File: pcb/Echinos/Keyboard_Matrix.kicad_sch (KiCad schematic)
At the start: 40 parts, among them J5 Joystick

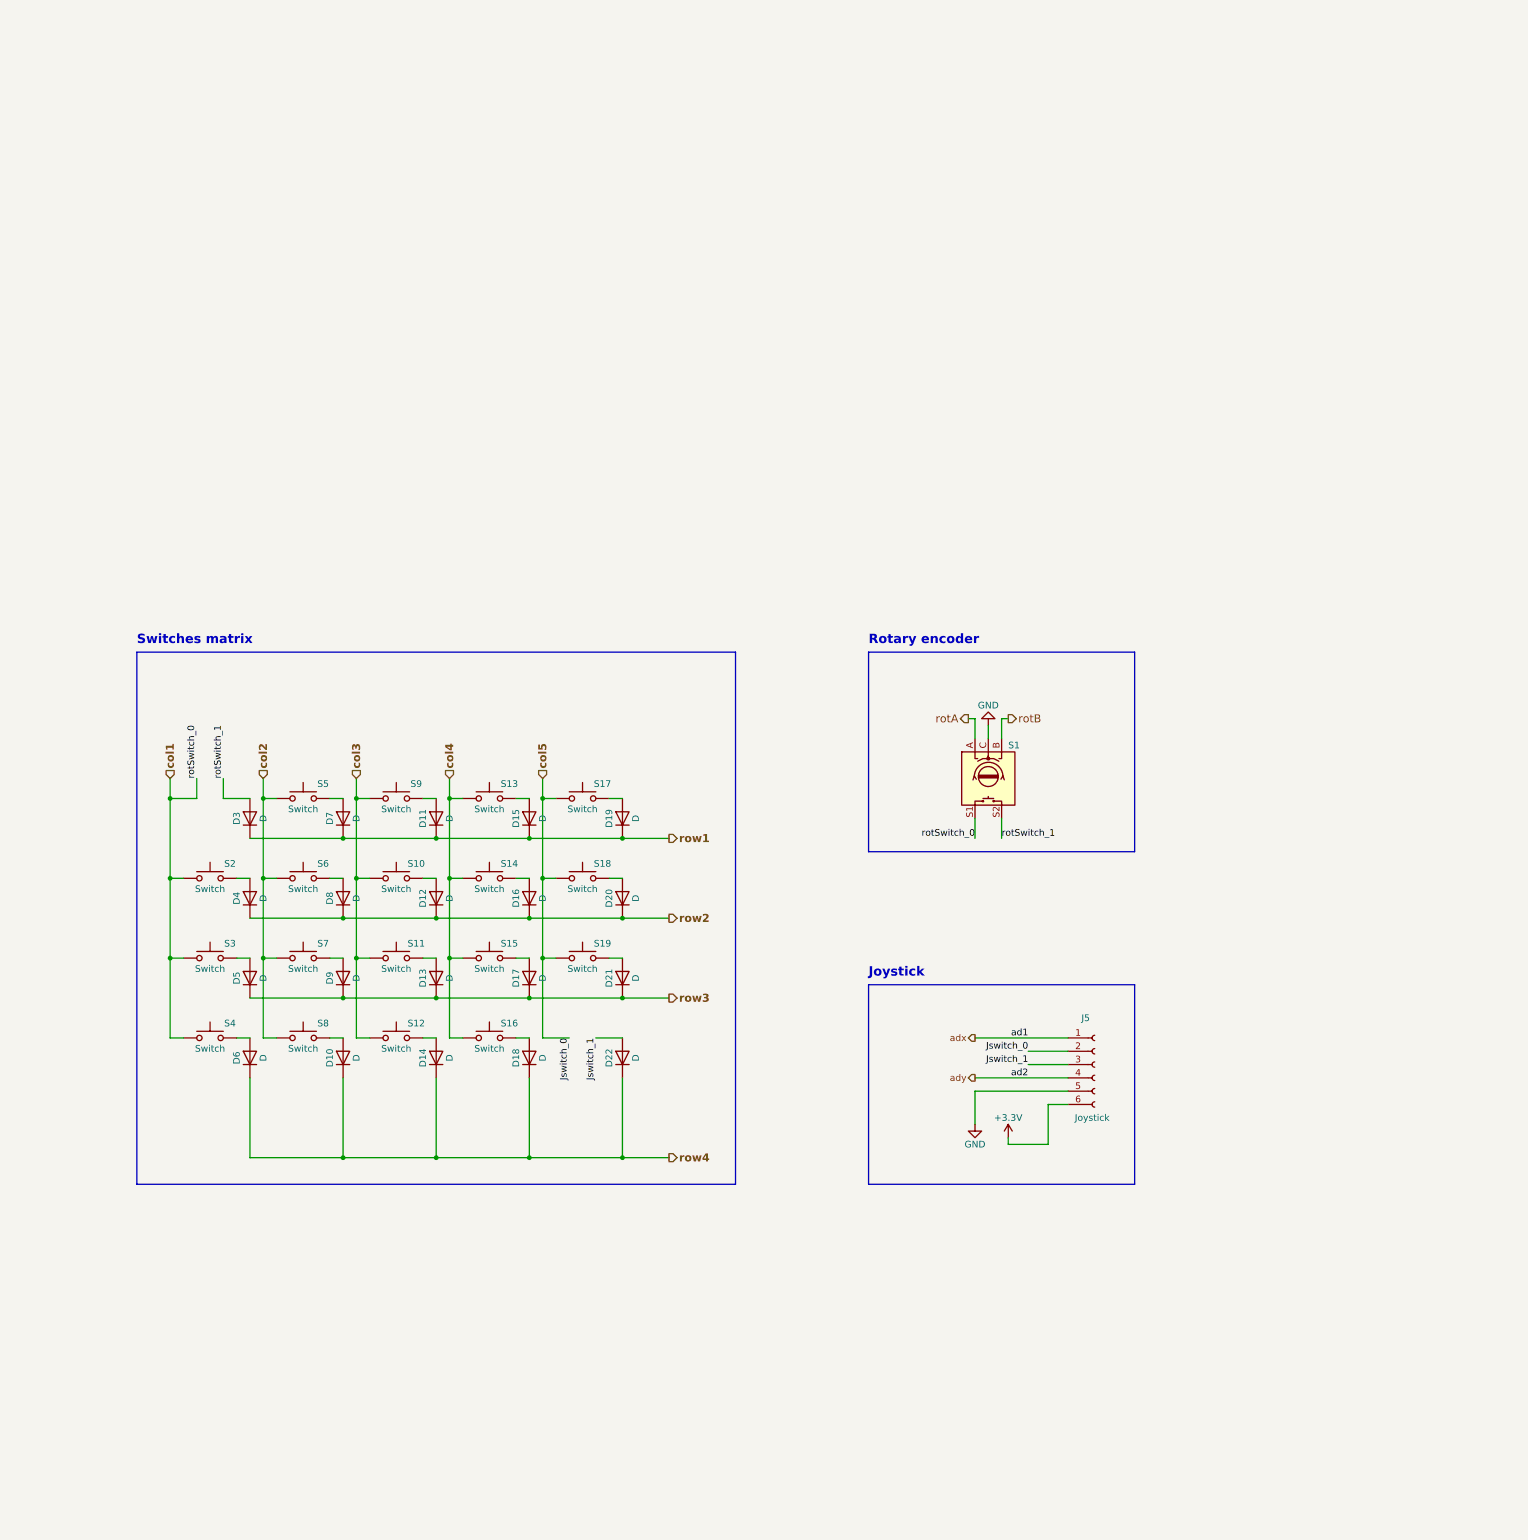
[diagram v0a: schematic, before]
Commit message: ✨ [PCB] - Continue draft schematic by adding per key RGB LED.
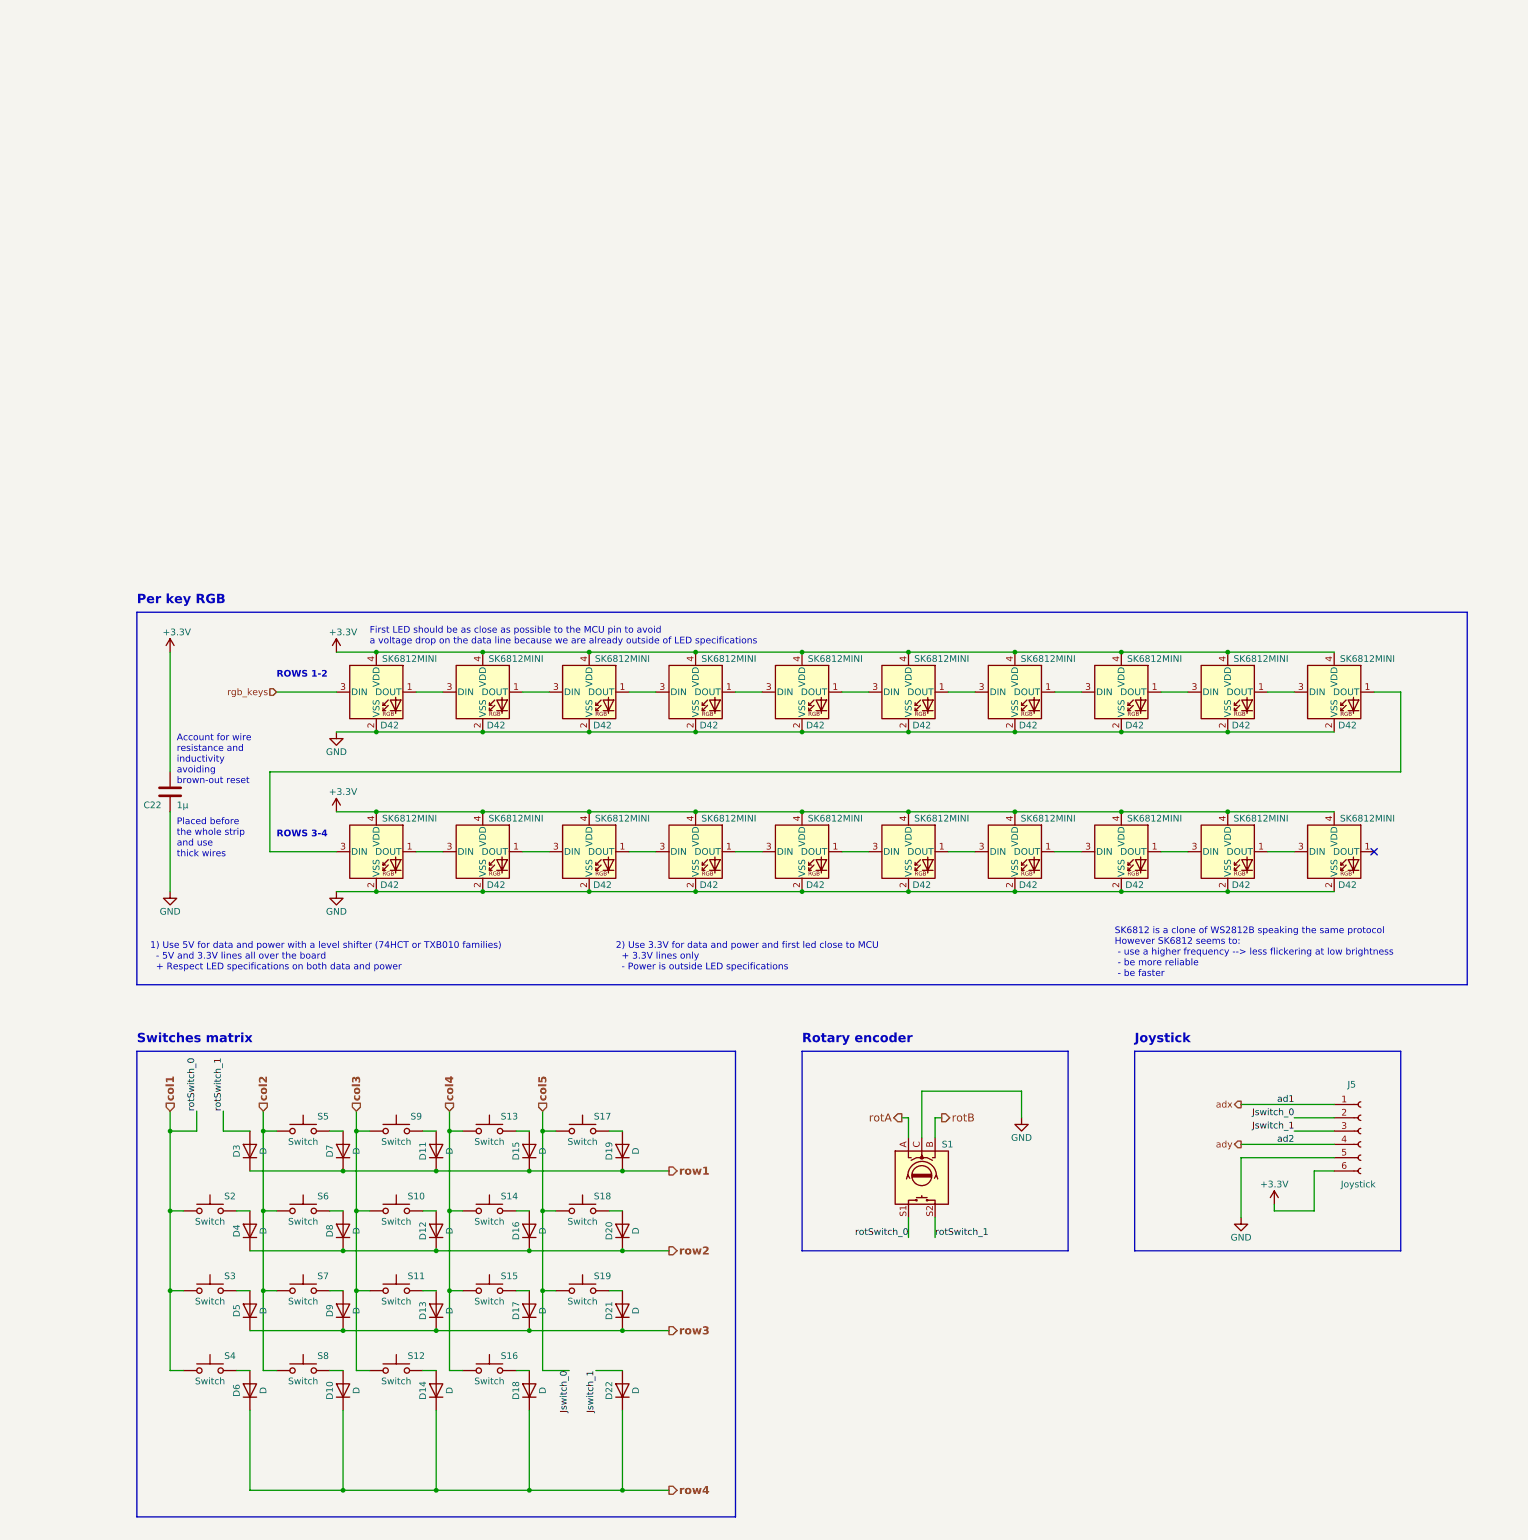
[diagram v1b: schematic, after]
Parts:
- added C22: 1µ, Capacitor_SMD:C_0402_1005Metric, symbol Device:C
- added D42 (x20): SK6812MINI, LED_SMD:LED_SK6812MINI_PLCC4_3.5x3.5mm_P1.75mm, symbol LED:SK6812MINI
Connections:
- net +3V3: now also C22.1, D42.4 (VDD), D42.4 (VDD), D42.4 (VDD), D42.4 (VDD), D42.4 (VDD), D42.4 (VDD), D42.4 (VDD), D42.4 (VDD), D42.4 (VDD), D42.4 (VDD), D42.4 (VDD), D42.4 (VDD), D42.4 (VDD), D42.4 (VDD), D42.4 (VDD), D42.4 (VDD), D42.4 (VDD), D42.4 (VDD), D42.4 (VDD), D42.4 (VDD)
- net GND: now also C22.2, D42.2 (VSS), D42.2 (VSS), D42.2 (VSS), D42.2 (VSS), D42.2 (VSS), D42.2 (VSS), D42.2 (VSS), D42.2 (VSS), D42.2 (VSS), D42.2 (VSS), D42.2 (VSS), D42.2 (VSS), D42.2 (VSS), D42.2 (VSS), D42.2 (VSS), D42.2 (VSS), D42.2 (VSS), D42.2 (VSS), D42.2 (VSS), D42.2 (VSS)
- new net: D42.1 (DOUT), D42.3 (DIN) (x19)
- new net rgb_keys: D42.3 (DIN)
- no-connect marks 0 -> 1
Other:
- note added: "1) Use 5V for data and power with a level shifter (74HCT or TXB010 families) - 5V and 3.3V lines all over the board + Respect LED specifications on both data and power"
- note added: "2) Use 3.3V for data and power and first led close to MCU + 3.3V lines only - Power is outside LED specifications"
- note added: "Account for wire resistance and inductivity avoiding brown-out reset"
- note added: "First LED should be as close as possible to the MCU pin to avoid a voltage drop on the data line because we are already outside of LED specifications"
- note added: "Per key RGB"
- note added: "Placed before the whole strip and use thick wires"
- note added: "ROWS 1-2"
- note added: "ROWS 3-4"
- note added: "SK6812 is a clone of WS2812B speaking the same protocol However SK6812 seems to: - use a higher frequency --> less flickering at low brightness - be more reliable - be faster"
- moved on the sheet: D10, D11, D12, D13, D14, D15, D16, D17, D18, D19, D20, D21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

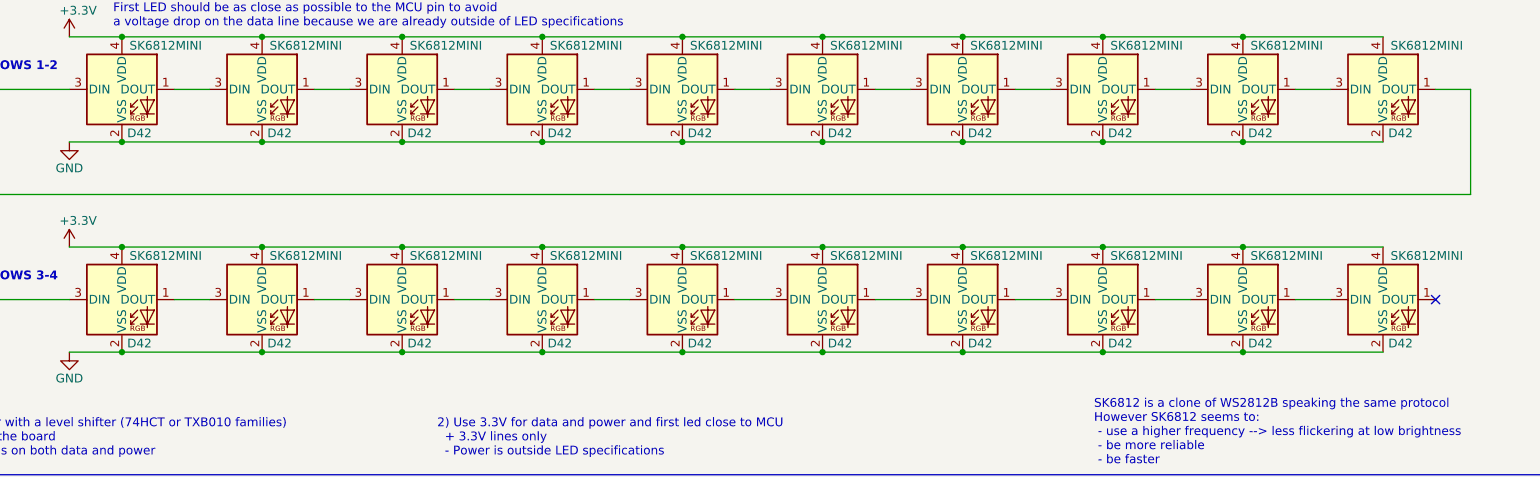
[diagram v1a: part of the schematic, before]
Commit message: ♻️ [PCB] - Remove symbol instances linking to other projets due to copy and paste of component symbol.
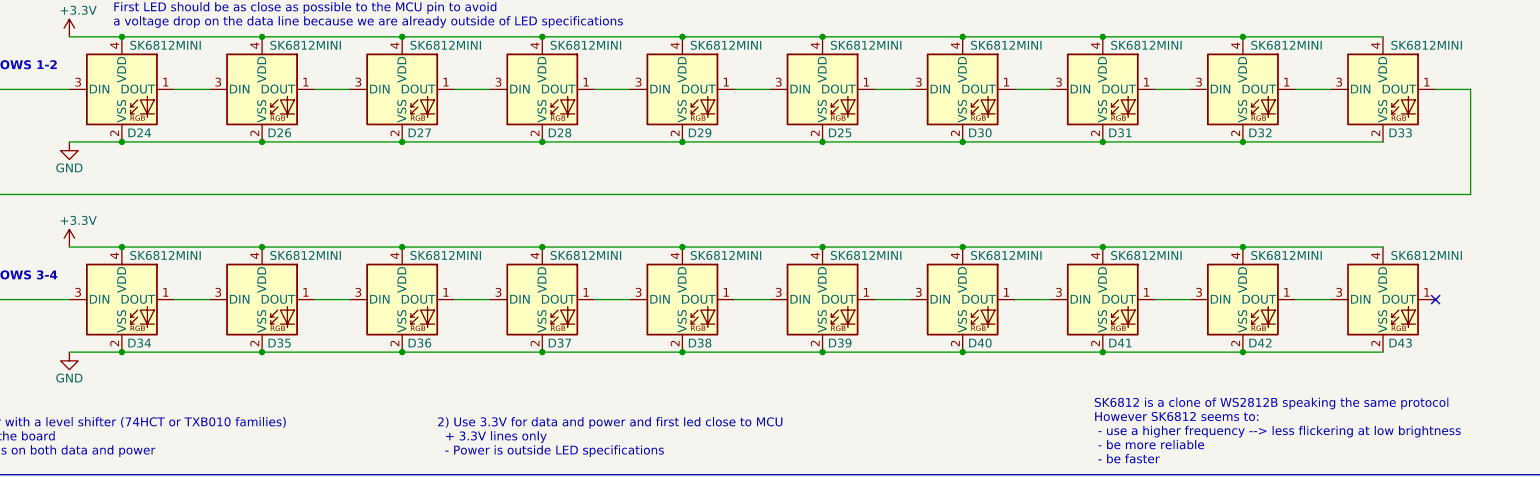
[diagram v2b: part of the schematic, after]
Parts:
- renumbered D42 to D24, D42 to D25, D42 to D26, D42 to D27, D42 to D28, D42 to D29, D42 to D30, D42 to D31, D42 to D32, D42 to D33, D42 to D34, D42 to D35, D42 to D36, D42 to D37, D42 to D38, D42 to D39, D42 to D40, D42 to D41, D42 to D43

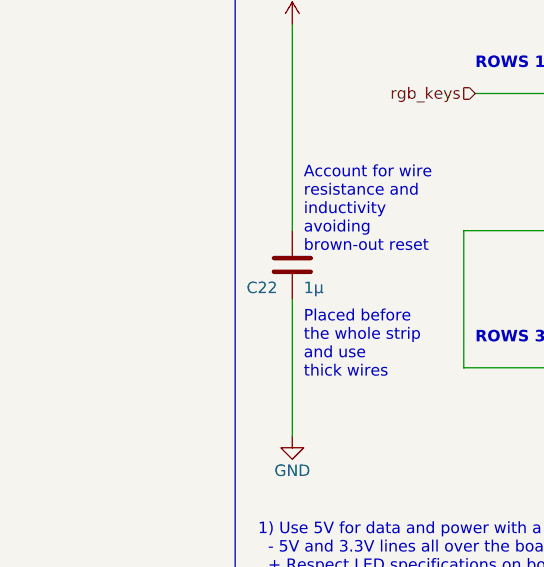
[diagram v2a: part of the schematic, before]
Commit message: ♻️ [PCB] - Add ferrite bead between shield and ground. Assign hand solder footprints whenever possible. Complete footprint assignation.
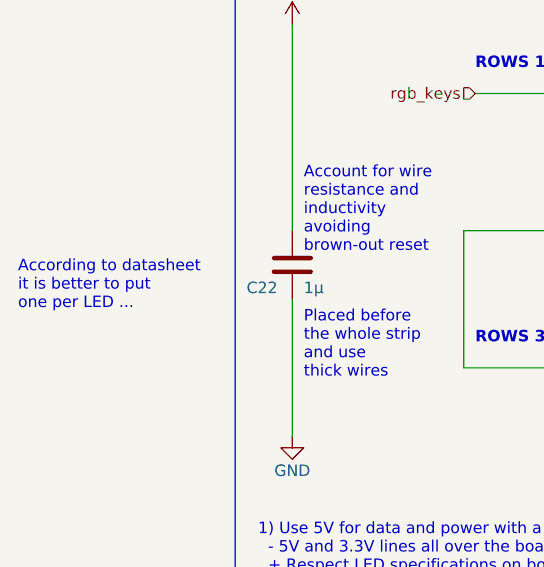
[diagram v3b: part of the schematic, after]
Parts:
- J5: footprint (none) -> Fuse:Fuse_0603_1608Metric_Pad1.05x0.95mm_HandSolder
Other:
- note added: "According to datasheet it is better to put one per LED ..."
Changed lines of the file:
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@@
+    (effects (font (size 1.27 1.27)) (justify left bottom))
+  )
+  (text "According to datasheet \nit is better to put\none per LED ..."
+    (at 1.27 57.15 0)
     (effects (font (size 1.27 1.27)) (justify left bottom))
   )
@@
       (effects (font (size 1.27 1.27)) (justify left))
     )
-    (property "Footprint" "" (at 259.08 116.84 0)
-      (effects (font (size 1.27 1.27)) hide)
-    )
+    (property "Footprint" "Fuse:Fuse_0603_1608Metric_Pad1.05x0.95mm_HandSolder" (at 259.08 116.84 0)
+      (effects (font (size 1.27 1.27)) hide)
+    )
